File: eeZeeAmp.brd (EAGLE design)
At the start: 18.8 x 13.7 mm, 20 parts, among them IC1 LM386

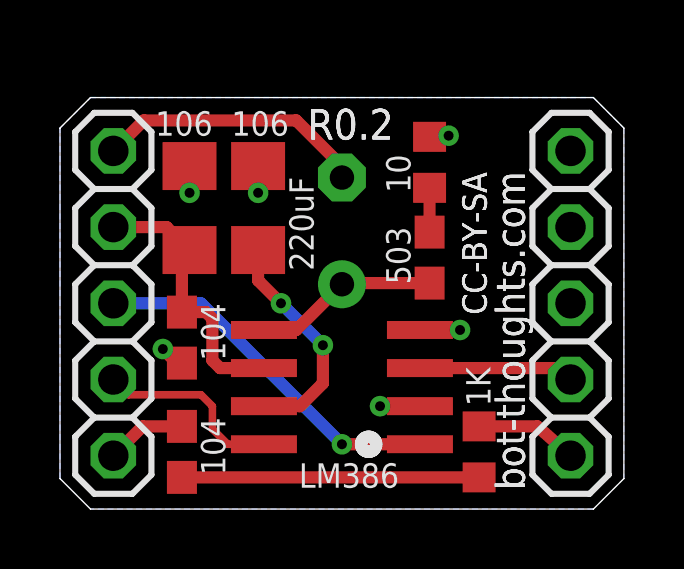
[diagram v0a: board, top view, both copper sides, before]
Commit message: Changed 503 cap to more common value 473
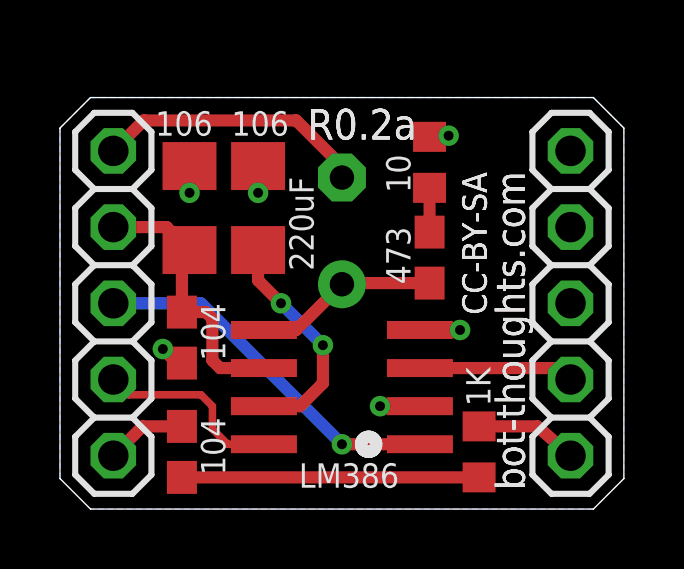
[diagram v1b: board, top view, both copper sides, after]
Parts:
- C3: value 503 -> 473
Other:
- board text added: "473"
- board text added: "R0.2a"
- board text removed: "503"
- board text removed: "R0.2"
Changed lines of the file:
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@@
 <layer number="19" name="Unrouted" color="6" fill="1" visible="yes" active="yes"/>
 <layer number="20" name="Dimension" color="15" fill="1" visible="yes" active="yes"/>
-<layer number="21" name="tPlace" color="7" fill="1" visible="no" active="yes"/>
-<layer number="22" name="bPlace" color="7" fill="1" visible="no" active="yes"/>
-<layer number="23" name="tOrigins" color="15" fill="1" visible="no" active="yes"/>
-<layer number="24" name="bOrigins" color="15" fill="1" visible="no" active="yes"/>
-<layer number="25" name="tNames" color="7" fill="1" visible="no" active="yes"/>
-<layer number="26" name="bNames" color="7" fill="1" visible="no" active="yes"/>
-<layer number="27" name="tValues" color="7" fill="1" visible="no" active="yes"/>
-<layer number="28" name="bValues" color="7" fill="1" visible="no" active="yes"/>
+<layer number="21" name="tPlace" color="7" fill="1" visible="yes" active="yes"/>
+<layer number="22" name="bPlace" color="7" fill="1" visible="yes" active="yes"/>
+<layer number="23" name="tOrigins" color="15" fill="1" visible="yes" active="yes"/>
+<layer number="24" name="bOrigins" color="15" fill="1" visible="yes" active="yes"/>
+<layer number="25" name="tNames" color="7" fill="1" visible="yes" active="yes"/>
+<layer number="26" name="bNames" color="7" fill="1" visible="yes" active="yes"/>
+<layer number="27" name="tValues" color="7" fill="1" visible="yes" active="yes"/>
+<layer number="28" name="bValues" color="7" fill="1" visible="yes" active="yes"/>
 <layer number="29" name="tStop" color="7" fill="3" visible="yes" active="yes"/>
 <layer number="30" name="bStop" color="7" fill="6" visible="yes" active="yes"/>
@@
 <wire x1="1.016" y1="13.716" x2="0" y2="12.7" width="0" layer="20"/>
 <text x="12.827" y="4.064" size="1.016" layer="26" font="vector" ratio="12" rot="MR0">eeZeeAmp</text>
-<text x="8.255" y="12.319" size="1.016" layer="25" font="vector" ratio="12">R0.2</text>
+<text x="8.255" y="12.319" size="1.016" layer="25" font="vector" ratio="12">R0.2a</text>
 <text x="15.494" y="0.635" size="0.9652" layer="25" font="vector" ratio="12" rot="R90">bot-thoughts.com</text>
 <circle x="10.287" y="2.159" radius="0.254" width="0.4064" layer="21"/>
@@
 <vertex x="9.2186" y="1.598903125"/>
 </polygon>
-<text x="8.255" y="12.319" size="1.016" layer="121" font="vector" ratio="20">R0.2</text>
+<text x="8.255" y="12.319" size="1.016" layer="121" font="vector" ratio="20">R0.2a</text>
 <text x="15.494" y="0.635" size="0.9652" layer="121" font="vector" ratio="22" rot="R90">bot-thoughts.com</text>
 <text x="14.224" y="6.477" size="0.8128" layer="121" font="vector" ratio="25" rot="R90">CC-BY-SA</text>
@@
 <text x="8.456396875" y="7.9446625" size="0.8128" layer="121" font="vector" ratio="25" rot="R90">220uF</text>
 <text x="4.699" y="3.048" size="0.8128" layer="121" font="vector" ratio="25" rot="R270">104</text>
-<text x="11.684" y="7.493" size="0.8128" layer="121" font="vector" ratio="25" rot="R90">503</text>
+<text x="11.684" y="7.493" size="0.8128" layer="121" font="vector" ratio="25" rot="R90">473</text>
 <text x="3.175" y="12.446" size="0.8128" layer="121" font="vector" ratio="25">106</text>
 <text x="5.715" y="12.446" size="0.8128" layer="121" font="vector" ratio="25">106</text>
@@
 <attribute name="VALUE" x="4.699" y="3.048" size="0.8128" layer="27" font="vector" rot="R270"/>
 </element>
-<element name="C3" library="rcl" package="C0603" value="503" x="12.319" y="8.382" smashed="yes" rot="R90">
+<element name="C3" library="rcl" package="C0603" value="473" x="12.319" y="8.382" smashed="yes" rot="R90">
 <attribute name="VALUE" x="11.684" y="7.493" size="0.8128" layer="27" font="vector" rot="R90"/>
 </element>
